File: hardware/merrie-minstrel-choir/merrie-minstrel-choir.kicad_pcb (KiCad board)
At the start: 2 copper layers, 35 x 55 mm, 23 parts, among them J1 USB_C, J2 Bell_Interface, J3 UART, U1 ESP32-S3-WROOM-1-N8, U2 AZ1117-3.3, U4 USBLC6-2SC6

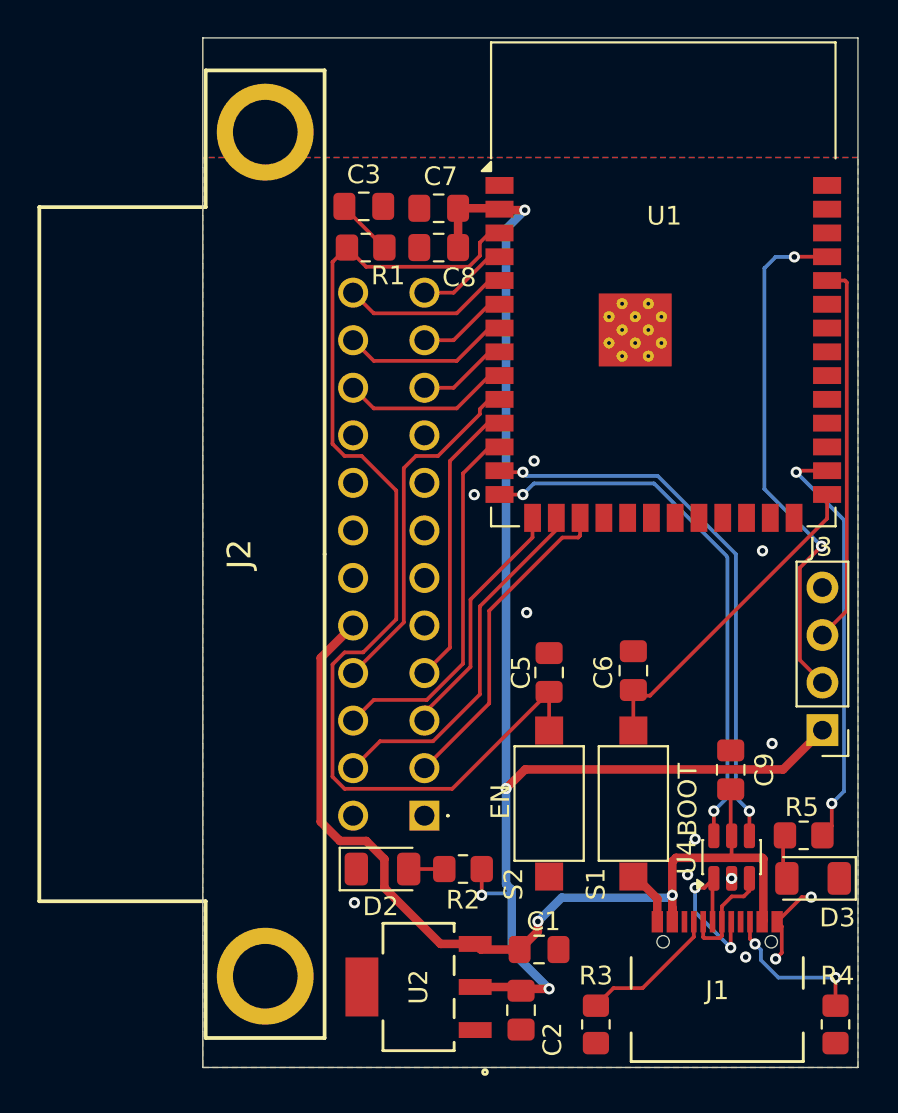
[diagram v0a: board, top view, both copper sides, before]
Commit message: Choir board rev 2: fix EN pull-up, bottom-mount J2, shrink outline
- EN: R1 now pulls EN to +3.3V and C3 sits from EN to GND (rev 1 had
  R1 and C3 in series to GND with no pull-up).
- J2 card-edge socket moved to the bottom side in the same slot
  position. The upside-down socket maps card finger n to pin 25-n, so the
  schematic is re-pinned and every bell still reaches the same GPIO.
- Outline 33.5 x 53 mm (was 35 x 55), inside the rev 1 outline, with
  USB-C and the J2 mounting holes unmoved.
- Re-routed with Freerouting; GND trace cleanup guarded by DRC.
  Scripts and the DSN/SES job are in route/.

Co-Authored-By: Claude Opus 5.5 <noreply@anthropic.com>
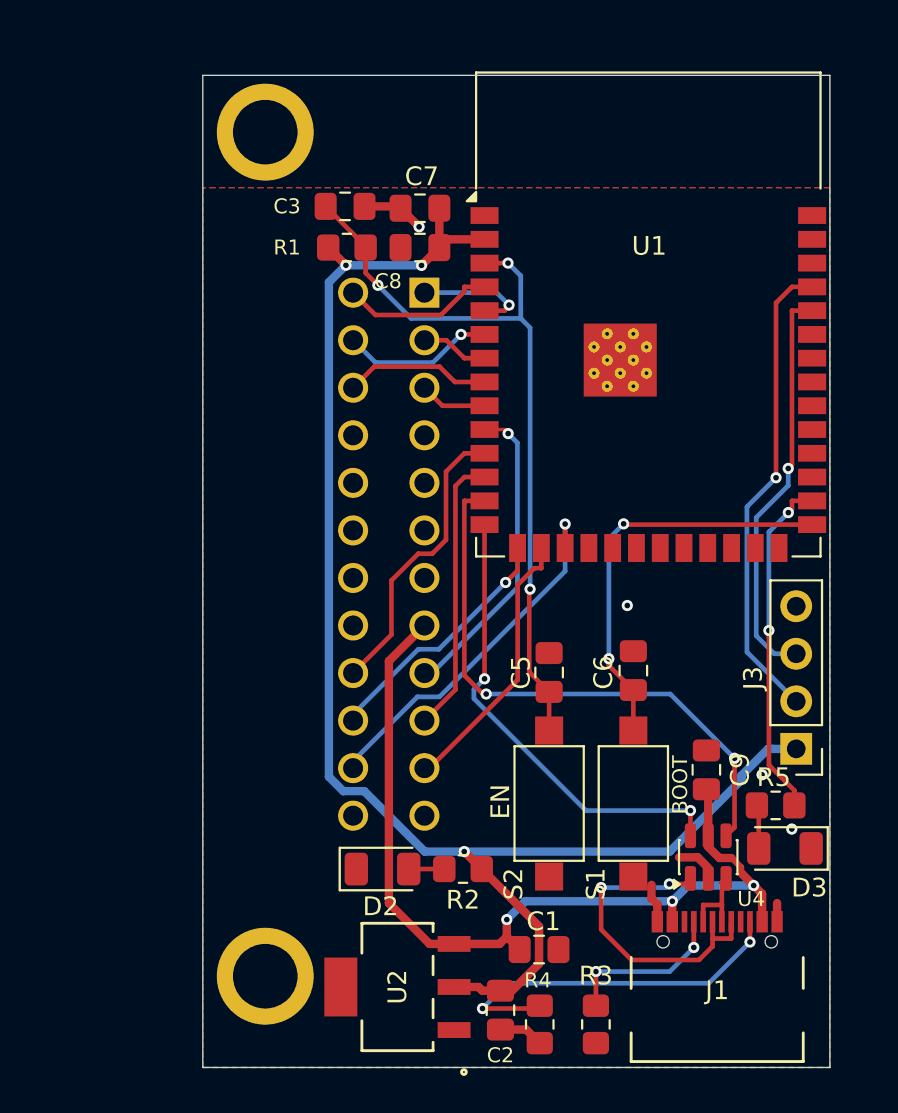
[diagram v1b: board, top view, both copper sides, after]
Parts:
- J2: moved to B.Cu
- moved J2 27.9 mm to (58.8, 66.6), turned to -90 degrees
- moved R4 15.8 mm to (65.0, 105.7)
- moved D3 2.19 mm to (78.1, 96.3)
- moved R5 2.19 mm to (77.6, 94.0)
- moved U1 1.80 mm to (70.8, 67.8)
- moved J3 1.72 mm to (78.7, 91.0)
- moved C9 1.30 mm to (73.9, 92.1)
- moved U4 1.25 mm to (74.0, 96.8)
- moved U2 1.12 mm to (57.4, 103.7)
- moved C2 1.10 mm to (62.9, 104.9)
- moved C3 1.00 mm to (54.6, 62.0)
- moved C7 1.00 mm to (58.6, 62.1)
- moved C8 1.00 mm to (58.6, 64.2)
- moved R1 1.00 mm to (54.7, 64.2)
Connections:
- C3 pad 1: Net-(C3-Pad1) -> /EN
- J2 pad 1: unconnected-(J2-Pad1) -> /Bell_12
- J2 pad 10: VCC -> unconnected-(J2-Pad10)
- J2 pad 15: unconnected-(J2-Pad15) -> VCC
- J2 pad 16: unconnected-(J2-Pad16) -> GND
- J2 pad 17: unconnected-(J2-Pad17) -> /Bell_9
- J2 pad 18: unconnected-(J2-Pad18) -> /Bell_3
- J2 pad 19: /Bell_4 -> /Bell_8
- J2 pad 2: unconnected-(J2-Pad2) -> /Bell_6
- J2 pad 20: /Bell_10 -> /Bell_2
- J2 pad 21: /Bell_5 -> /Bell_7
- J2 pad 22: /Bell_11 -> /Bell_1
- J2 pad 23: /Bell_6 -> unconnected-(J2-Pad23)
- J2 pad 24: /Bell_12 -> unconnected-(J2-Pad24)
- J2 pad 3: /Bell_1 -> /Bell_11
- J2 pad 4: /Bell_7 -> /Bell_5
- J2 pad 5: /Bell_2 -> /Bell_10
- J2 pad 6: /Bell_8 -> /Bell_4
- J2 pad 7: /Bell_3 -> unconnected-(J2-Pad7)
- J2 pad 8: /Bell_9 -> unconnected-(J2-Pad8)
- J2 pad 9: GND -> unconnected-(J2-Pad9)
- R1 pad 1: /EN -> +3.3V
- R1 pad 2: Net-(C3-Pad1) -> /EN
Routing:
- net /EN: track 58.8 -> 40.9 mm, vias 0 -> 3
- net /CC2: track 8.16 -> 20.0 mm
- net /D+: track 8.94 -> 17.4 mm
- net +3.3V: track 74.0 -> 81.0 mm, vias 4 -> 3
- net /Bell_11: track 9.00 -> 3.61 mm
- net /Bell_10: track 9.00 -> 3.61 mm
- net /Bell_8: track 19.8 -> 15.0 mm
- net /Bell_7: track 19.5 -> 14.7 mm
- net /USB_D+: track 29.2 -> 24.9 mm
- net /LED_0: track 22.6 -> 18.4 mm
- net /GPIO_0: track 17.8 -> 22.0 mm, vias 0 -> 2
- net VCC: track 52.1 -> 48.6 mm, vias 2 -> 3
- net /Bell_6: track 4.81 -> 8.28 mm
- net /Bell_5: track 4.81 -> 8.13 mm, vias 0 -> 1
- net Net-(C3-Pad1): track 3.09 -> 0.00 mm
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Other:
- board size 35 x 55 mm -> 33.5 x 53 mm

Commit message: Choir rev 2: 0805 LEDs, 0603 resistors, J2 at the board edge
- D2/D3 to LED_0805, R1-R5 to R_0603 (hand-solder pads).
- J2 footprint without its mounting holes (card_edge_395024559212_noMH);
  the socket ears hang off the board, so the left edge moves in to
  0.5 mm outside the outer pin row. Board is now 26.8 x 53 mm.
- EN cap C3 moves next to C5; R1/C7/C8 sit in a row above J2.
- Re-routed and GND traces trimmed under DRC guard.

Co-Authored-By: Claude Opus 5.5 <noreply@anthropic.com>
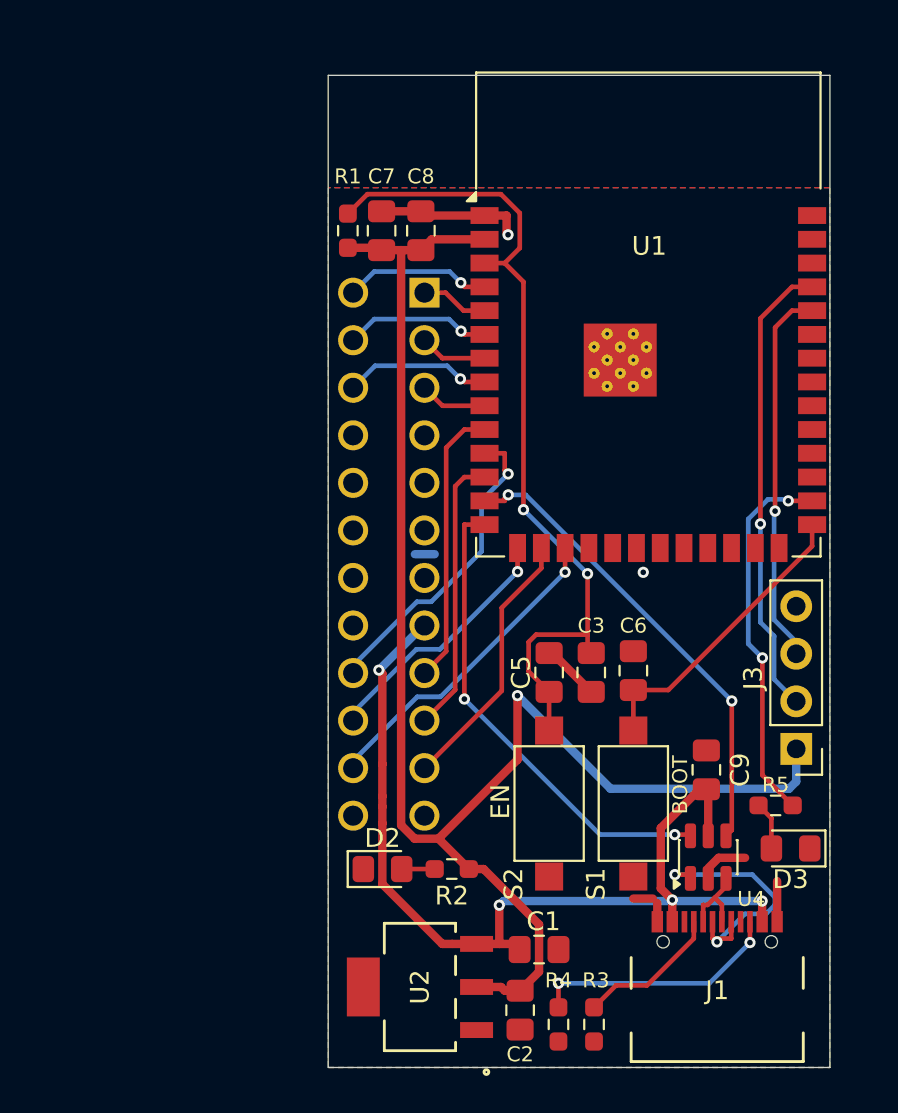
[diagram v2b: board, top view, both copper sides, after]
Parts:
- D2, D3: footprint LED_SMD:LED_1206_3216Metric -> LED_SMD:LED_0805_2012Metric_Pad1.15x1.40mm_HandSolder
- J2: footprint footprints:card_edge_395024559212 -> footprints:card_edge_395024559212_noMH
- R1, R2, R3, R4, R5: footprint Resistor_SMD:R_0805_2012Metric_Pad1.20x1.40mm_HandSolder -> Resistor_SMD:R_0603_1608Metric_Pad0.98x0.95mm_HandSolder
- moved C3 28.2 mm to (67.8, 86.9), turned to -90 degrees
- moved C7 2.38 mm to (56.5, 63.3), turned to 90 degrees
- moved U2 1.20 mm to (58.6, 103.7)
- moved C2 1.05 mm to (64.0, 104.9)
- moved R4 1.00 mm to (66.0, 105.7)
- moved C8 0.90 mm to (58.6, 63.3), turned to 90 degrees
- moved R1 0.90 mm to (54.8, 63.3), turned to 90 degrees
- moved R2 0.60 mm to (60.3, 97.4)
- moved D3 0.30 mm to (78.4, 96.3)
- moved R3 0.10 mm to (67.9, 105.7)
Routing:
- net GND: track 10.5 -> 18.4 mm, vias 4 -> 2
- net /CC2: track 20.0 -> 13.5 mm
- net /GPIO_0: track 22.0 -> 16.0 mm, vias 2 -> 0
- net /USB_D-: track 31.0 -> 25.3 mm
- net /EN: track 40.9 -> 45.4 mm, vias 3 -> 2
- net VCC: track 48.6 -> 52.2 mm, vias 3 -> 4
- net /D+: track 17.4 -> 14.1 mm
- net /Bell_12: track 6.27 -> 3.61 mm, vias 1 -> 0
- net /Bell_1: track 19.7 -> 17.2 mm
- net /LED_0: track 18.4 -> 20.2 mm
- net /Bell_9: track 16.6 -> 15.0 mm, vias 1 -> 0
- net /RXD0: track 21.8 -> 20.3 mm
- net +3.3V: track 81.0 -> 82.5 mm, vias 3 -> 1
- net /CC1: track 8.96 -> 7.75 mm, vias 2 -> 0
- net /Bell_3: track 15.7 -> 16.8 mm, vias 0 -> 1
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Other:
- board size 33.5 x 53 mm -> 26.8 x 53 mm

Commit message: Choir rev 2: route USB as a coupled pair, top edge at the antenna
- ESD (U4) to ESP32 USB runs as a locked B.Cu pair, 0.3 mm / 0.2 mm gap,
  1.1 mm skew; J1 to U4 kept as short as the receptacle pinout allows.
- Board top edge moves to y 61 (antenna overhangs), from the edit made
  in KiCad. R1 moves next to C5/C3 so the 3V3 caps' labels fit.
- import_ses.py drops zero-length stubs and widens tracks necked below
  0.1524 mm; usb_pair.py added to the route pipeline.

Co-Authored-By: Claude Opus 5.5 <noreply@anthropic.com>
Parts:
- moved R1 25.2 mm to (63.6, 86.9)
- moved C7 0.55 mm to (56.0, 63.3)
- moved C8 0.55 mm to (58.1, 63.3)
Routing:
- net /EN: track 45.4 -> 36.4 mm
- net GND: track 18.4 -> 10.6 mm, vias 2 -> 4
- net /D+: track 14.1 -> 6.95 mm
- net VCC: track 52.2 -> 56.4 mm, vias 4 -> 5
- net +3.3V: track 82.5 -> 86.3 mm, vias 1 -> 2
- net /Bell_9: track 15.0 -> 17.6 mm, vias 0 -> 1
- net /Bell_12: track 3.61 -> 6.22 mm, vias 0 -> 1
- net /USB_D+: track 25.5 -> 23.6 mm
- net /LED_0: track 20.2 -> 19.1 mm
- net /Bell_11: track 3.61 -> 4.59 mm
- net /TXD0: track 24.7 -> 25.6 mm, vias 1 -> 2
- net /Bell_3: track 16.8 -> 15.9 mm
- net /CC2: track 13.5 -> 12.8 mm
- net /USB_D-: track 25.3 -> 24.7 mm
- net /Bell_6: track 7.85 -> 8.33 mm, vias 1 -> 0
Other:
- board size 26.8 x 53 mm -> 26.8 x 47 mm

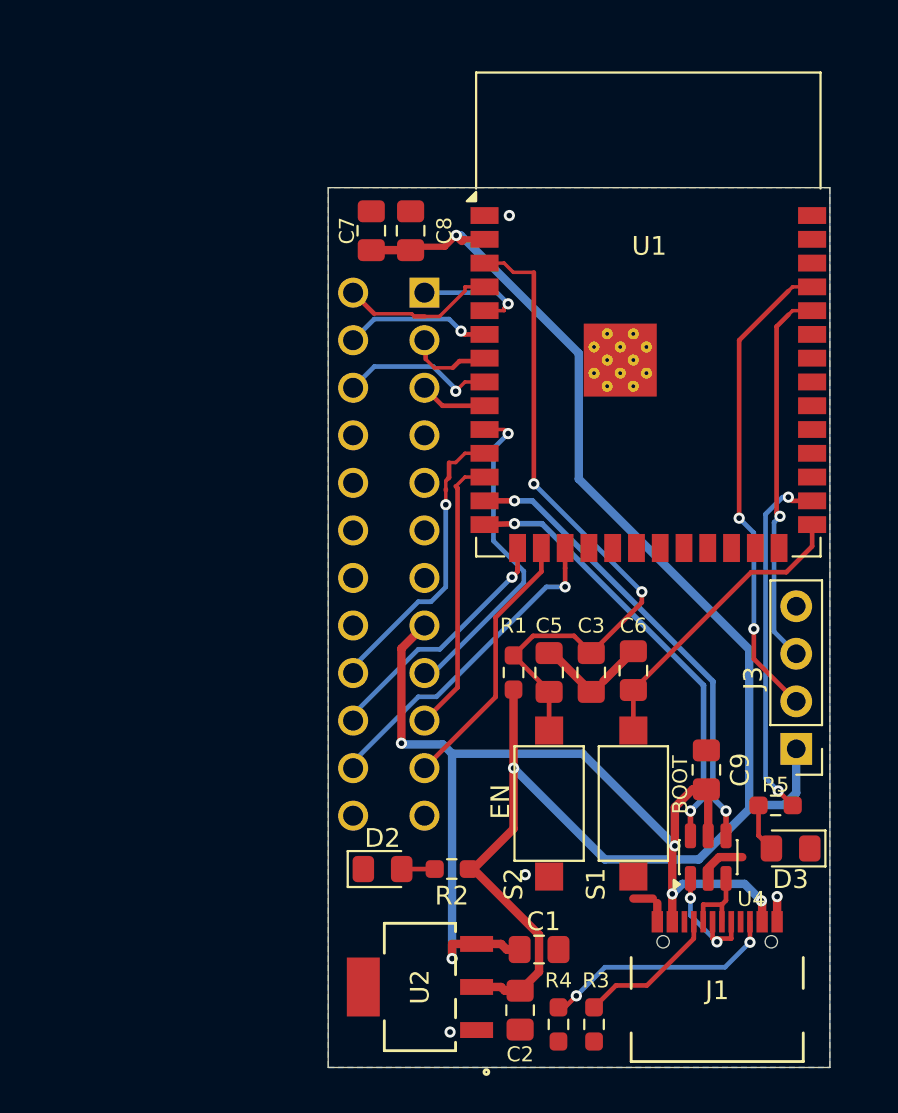
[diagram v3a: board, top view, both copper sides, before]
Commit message: Choir rev 2: R/C to the back, shrink to 26.8 x 37 mm, schematic fixes
Layout:
- Every resistor and capacitor moves to the back, behind the part it serves.
- The board shrinks to 26.8 x 37 mm. J1 moves up 10 mm, so the enclosure's
  USB-C opening has to move too.
- The J1/U4/C9 corner is hand-routed and locked; the rest is re-routed with
  Freerouting, and the redundant GND traces are removed.
- Silkscreen references are re-placed at the 0.8 mm minimum.
- New scripts: route/v3_layout.py, usb_v3.py, silk_v3.py.

Schematic:
- Adds R6, a 10k pull-up on GPIO0. BOOT stays, for serial flashing and as a
  user button.
- Removes the button caps C5 and C6.
- R2/R5 are now 1.5k, so the LEDs glow dimly.
- S1/S2 move to the TS-1088 footprint.
- ERC is clean: PWR_FLAGs added and pin types fixed in the vendor libraries.
- Adds a project-local sym-lib-table and fp-lib-table and a footprints.pretty
  library, plus a rebuilt symbol for the EDAC 395-024-559-212 socket.

Co-Authored-By: Claude Opus 5.5 <noreply@anthropic.com>
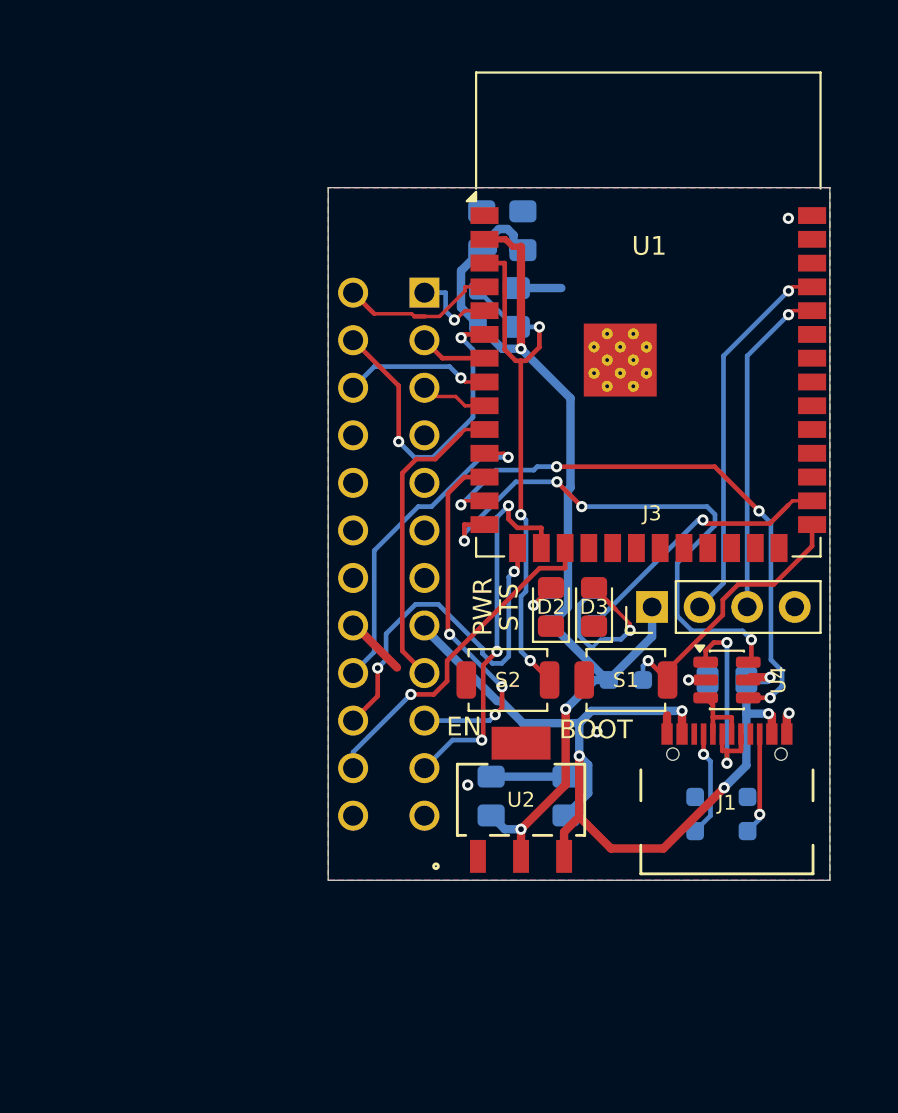
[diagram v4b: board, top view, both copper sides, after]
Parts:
- removed C5, C6: 0.1uF, Capacitor_SMD:C_0805_2012Metric_Pad1.18x1.45mm_HandSolder
- added R6: 10K, Resistor_SMD:R_0603_1608Metric_Pad0.98x0.95mm_HandSolder, B.Cu at (69.6, 87.3)
- C1, C2, C3, C7, C8, C9, R1, R3, R4: moved to B.Cu
- R2, R5: value 220 -> 1.5K; moved to B.Cu
- S1, S2: footprint Button_Switch_SMD:SW_SPST_CK_RS282G05A3 -> Button_Switch_SMD:SW_SPST_TS-1088-xR020
- moved C3 19.9 mm to (63.8, 67.4), turned to 90 degrees
- moved R1 19.6 mm to (61.7, 67.4)
- moved D2 16.6 mm to (65.6, 83.4), turned to 90 degrees
- moved D3 16.6 mm to (67.9, 83.4), turned to 90 degrees
- moved R4 15.1 mm to (76.1, 94.5), turned to 90 degrees
- moved R2 15.0 mm to (65.6, 83.4), turned to 90 degrees
- moved R5 14.4 mm to (67.9, 83.4), turned to 90 degrees
- moved R3 12.5 mm to (73.3, 94.5), turned to 90 degrees
- moved C2 11.5 mm to (62.4, 93.5), turned to 90 degrees
- moved U2 11.4 mm to (64.0, 93.7), turned to 0 degrees
- moved J3 10.8 mm to (71.0, 83.4), turned to 90 degrees
- moved J1 10.0 mm to (75.0, 93.9)
- moved U4 9.52 mm to (75.0, 87.3), turned to 0 degrees
- moved C1 8.32 mm to (66.4, 93.5), turned to 90 degrees
- moved C7 8.10 mm to (64.1, 63.3)
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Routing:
- net +3.3V: track 86.3 -> 58.4 mm, vias 2 -> 3
- net /Bell_5: track 7.83 -> 17.5 mm, vias 1 -> 2
- net /CC2: track 12.8 -> 5.45 mm, vias 2 -> 1
- net /Bell_2: track 13.5 -> 20.2 mm, vias 1 -> 2
- net Net-(D3-A): track 2.58 -> 9.20 mm, vias 0 -> 1
- net VCC: track 56.4 -> 49.8 mm
- net /USB_D-: track 24.7 -> 31.0 mm, vias 2 -> 4
- net /Bell_7: track 14.3 -> 20.5 mm, vias 0 -> 3
- net /USB_D+: track 23.6 -> 29.6 mm, vias 2 -> 4
- net /TXD0: track 25.6 -> 20.2 mm, vias 2 -> 1
- net /EN: track 36.4 -> 31.2 mm, vias 2 -> 3
- net /D+: track 6.95 -> 11.8 mm
- net /LED_0: track 19.1 -> 14.5 mm, vias 2 -> 1
- net /Bell_8: track 15.0 -> 19.4 mm, vias 0 -> 3
- net /RXD0: track 20.4 -> 17.9 mm
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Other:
- board size 26.8 x 47 mm -> 26.8 x 37 mm
- board text added: "PWR"
- board text added: "STS"
